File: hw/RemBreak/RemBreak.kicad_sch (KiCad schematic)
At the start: 4 parts, among them J1 Screw_Terminal_01x04, J2 Screw_Terminal_01x04

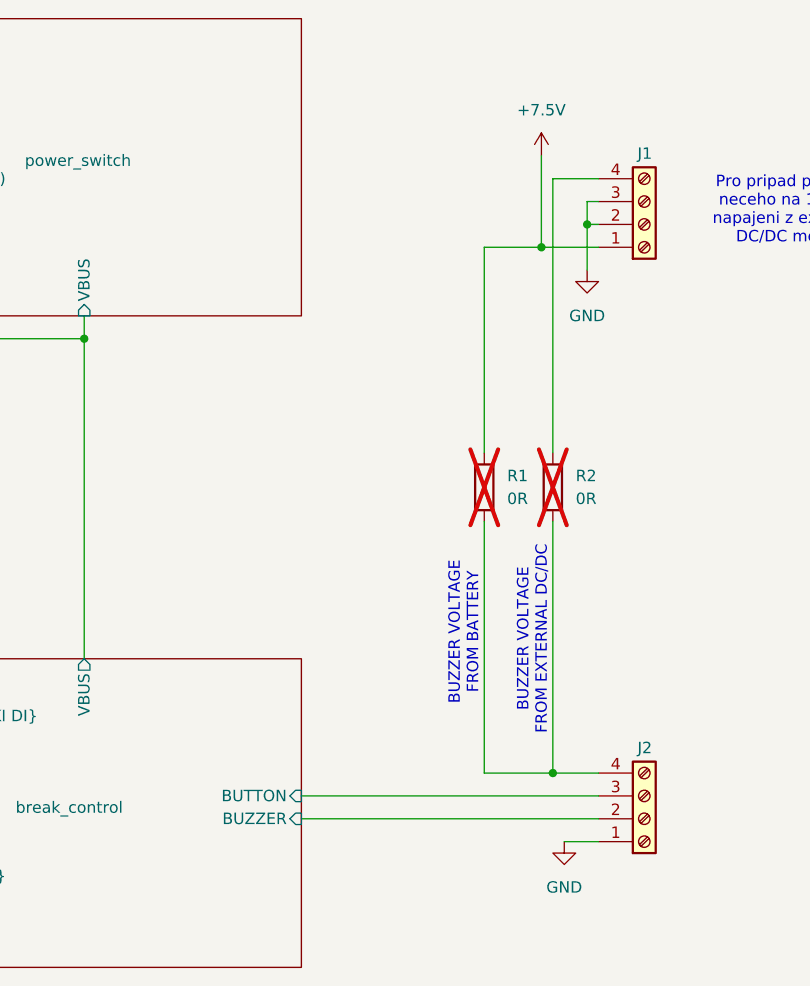
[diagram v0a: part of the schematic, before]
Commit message: partially reorganized components and routing
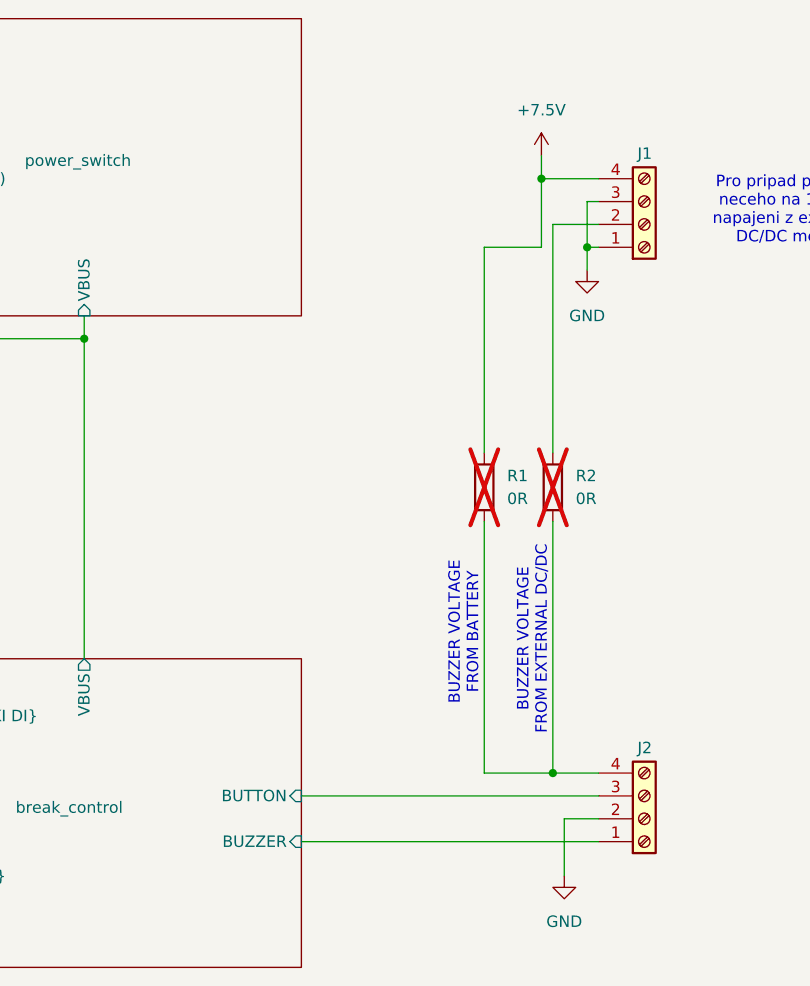
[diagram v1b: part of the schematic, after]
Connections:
- net +7.5V: now also J1.4 (Pin_4); no longer J1.1 (Pin_1)
- net GND: now also J1.1 (Pin_1), J2.2 (Pin_2); no longer J1.2 (Pin_2), J2.1 (Pin_1)
- net break_control/BUZZER: now also J2.1 (Pin_1); no longer J2.2 (Pin_2)
- net at R2.1: now also J1.2 (Pin_2); no longer J1.4 (Pin_4)
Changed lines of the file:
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@@
-	)
-	(junction
-		(at 234.95 68.58)
-		(diameter 0)
-		(color 0 0 0 0)
 	)
 	(junction
@@
 	)
 	(junction
-		(at 240.03 66.04)
+		(at 234.95 60.96)
 		(diameter 0)
 		(color 0 0 0 0)
@@
 	)
 	(junction
+		(at 240.03 68.58)
+		(diameter 0)
+		(color 0 0 0 0)
+	)
+	(junction
 		(at 236.22 127)
 		(diameter 0)
@@
 	(wire
 		(pts
+			(xy 208.28 134.62) (xy 241.3 134.62)
+		)
+		(stroke
+			(width 0)
+			(type default)
+		)
+	)
+	(wire
+		(pts
 			(xy 236.22 99.06) (xy 236.22 127)
 		)
@@
 	(wire
 		(pts
+			(xy 240.03 63.5) (xy 240.03 68.58)
+		)
+		(stroke
+			(width 0)
+			(type default)
+		)
+	)
+	(wire
+		(pts
 			(xy 82.55 129.54) (xy 161.29 129.54)
 		)
@@
 	(wire
 		(pts
-			(xy 234.95 68.58) (xy 241.3 68.58)
-		)
-		(stroke
-			(width 0)
-			(type default)
-		)
-	)
-	(wire
-		(pts
 			(xy 228.6 91.44) (xy 228.6 68.58)
 		)
@@
 	(wire
 		(pts
-			(xy 236.22 60.96) (xy 241.3 60.96)
-		)
-		(stroke
-			(width 0)
-			(type default)
-		)
-	)
-	(wire
-		(pts
-			(xy 240.03 66.04) (xy 240.03 63.5)
-		)
-		(stroke
-			(width 0)
-			(type default)
-		)
-	)
-	(wire
-		(pts
 			(xy 236.22 127) (xy 241.3 127)
 		)
@@
 	(wire
 		(pts
+			(xy 236.22 66.04) (xy 236.22 91.44)
+		)
+		(stroke
+			(width 0)
+			(type default)
+		)
+	)
+	(wire
+		(pts
+			(xy 240.03 68.58) (xy 241.3 68.58)
+		)
+		(stroke
+			(width 0)
+			(type default)
+		)
+	)
+	(wire
+		(pts
 			(xy 151.13 92.71) (xy 154.94 92.71)
 		)
@@
 	(wire
 		(pts
-			(xy 236.22 91.44) (xy 236.22 60.96)
+			(xy 234.95 60.96) (xy 241.3 60.96)
+		)
+		(stroke
+			(width 0)
+			(type default)
+		)
+	)
+	(wire
+		(pts
+			(xy 237.49 132.08) (xy 237.49 138.43)
 		)
 		(stroke
@@
 	(wire
 		(pts
+			(xy 234.95 60.96) (xy 234.95 68.58)
+		)
+		(stroke
+			(width 0)
+			(type default)
+		)
+	)
+	(wire
+		(pts
 			(xy 123.19 49.53) (xy 161.29 49.53)
 		)
@@
 	(wire
 		(pts
-			(xy 208.28 132.08) (xy 241.3 132.08)
-		)
-		(stroke
-			(width 0)
-			(type default)
-		)
-	)
-	(wire
-		(pts
-			(xy 234.95 58.42) (xy 234.95 68.58)
+			(xy 237.49 132.08) (xy 241.3 132.08)
+		)
+		(stroke
+			(width 0)
+			(type default)
+		)
+	)
+	(wire
+		(pts
+			(xy 234.95 58.42) (xy 234.95 60.96)
+		)
+		(stroke
+			(width 0)
+			(type default)
+		)
+	)
+	(wire
+		(pts
+			(xy 236.22 66.04) (xy 241.3 66.04)
 		)
 		(stroke
@@
 	(wire
 		(pts
-			(xy 237.49 134.62) (xy 241.3 134.62)
-		)
-		(stroke
-			(width 0)
-			(type default)
-		)
-	)
-	(wire
-		(pts
 			(xy 86.36 132.08) (xy 161.29 132.08)
 		)
@@
 	(wire
 		(pts
+			(xy 240.03 71.12) (xy 240.03 68.58)
+		)
+		(stroke
+			(width 0)
+			(type default)
+		)
+	)
+	(wire
+		(pts
 			(xy 86.36 92.71) (xy 86.36 132.08)
 		)
@@
 	(wire
 		(pts
-			(xy 240.03 71.12) (xy 240.03 66.04)
-		)
-		(stroke
-			(width 0)
-			(type default)
-		)
-	)
-	(wire
-		(pts
 			(xy 228.6 68.58) (xy 234.95 68.58)
 		)
@@
 		(pts
 			(xy 82.55 49.53) (xy 123.19 49.53)
-		)
-		(stroke
-			(width 0)
-			(type default)
-		)
-	)
-	(wire
-		(pts
-			(xy 240.03 66.04) (xy 241.3 66.04)
 		)
 		(stroke
@@
 	(symbol
 		(lib_id "power:GND")
-		(at 237.49 134.62 0)
+		(at 237.49 138.43 0)
 		(unit 1)
 		(exclude_from_sim no)
@@
 		(fields_autoplaced yes)
 		(property "Reference" "#PWR02"
-			(at 237.49 140.97 0)
+			(at 237.49 144.78 0)
 			(effects
 				(font
@@
 		)
 		(property "Value" "GND"
-			(at 237.49 139.7 0)
+			(at 237.49 143.51 0)
 			(effects
 				(font
@@
 		)
 		(property "Footprint" ""
-			(at 237.49 134.62 0)
+			(at 237.49 138.43 0)
 			(effects
 				(font
@@
 		)
 		(property "Datasheet" ""
-			(at 237.49 134.62 0)
+			(at 237.49 138.43 0)
 			(effects
 				(font
@@
 		)
 		(property "Description" "Power symbol creates a global label with name \"GND\" , ground"
-			(at 237.49 134.62 0)
+			(at 237.49 138.43 0)
 			(effects
 				(font
@@
 		)
 		(pin "BUZZER" input
-			(at 208.28 132.08 0)
-			(effects
-				(font
+			(at 208.28 134.62 0)
+			(effects
+				(font

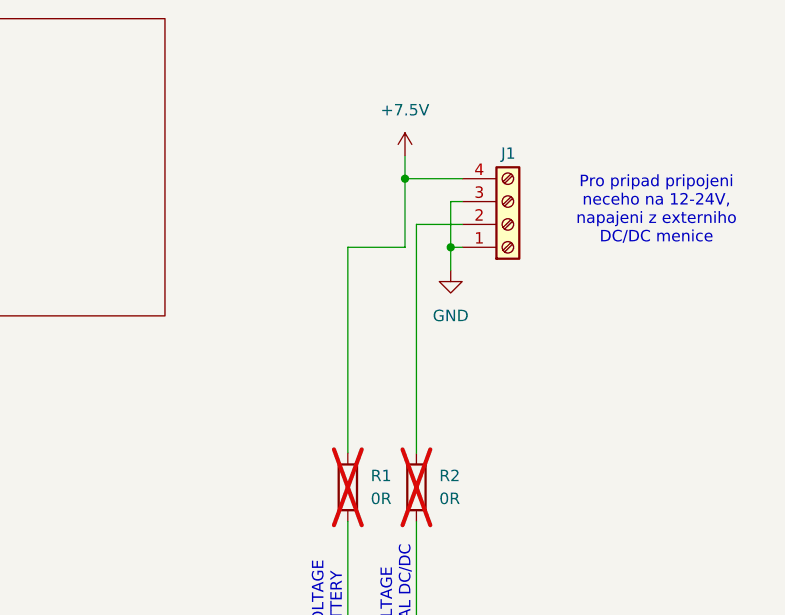
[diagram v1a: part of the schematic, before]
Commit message: middle part rerouted to fix the gnd connection
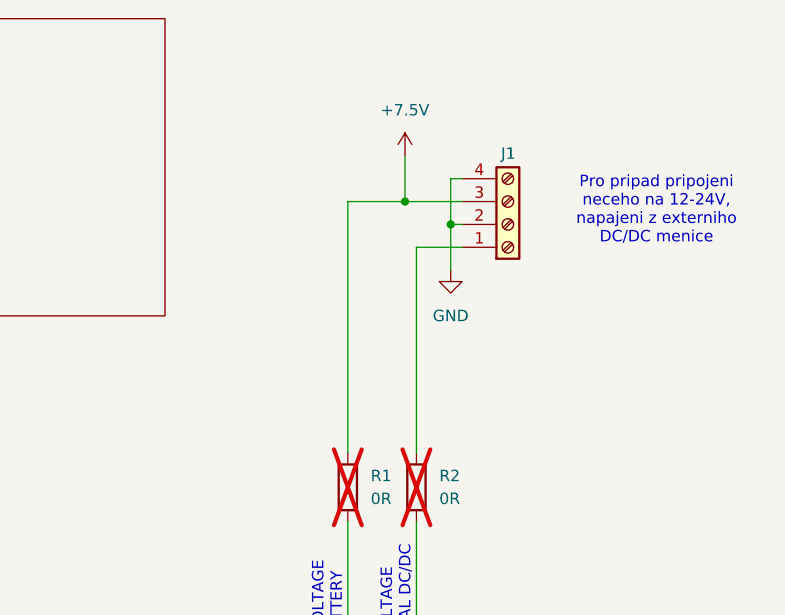
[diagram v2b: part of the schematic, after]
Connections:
- net +7.5V: now also J1.3 (Pin_3); no longer J1.4 (Pin_4)
- net GND: now also J1.2 (Pin_2), J1.4 (Pin_4); no longer J1.1 (Pin_1), J1.3 (Pin_3)
- net at R2.1: now also J1.1 (Pin_1); no longer J1.2 (Pin_2)
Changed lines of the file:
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@@
+	)
+	(junction
+		(at 234.95 63.5)
+		(diameter 0)
+		(color 0 0 0 0)
 	)
 	(junction
@@
 	)
 	(junction
-		(at 234.95 60.96)
-		(diameter 0)
-		(color 0 0 0 0)
-	)
-	(junction
 		(at 184.15 78.74)
 		(diameter 0)
@@
 	)
 	(junction
-		(at 240.03 68.58)
-		(diameter 0)
-		(color 0 0 0 0)
-	)
-	(junction
 		(at 236.22 127)
 		(diameter 0)
 		(color 0 0 0 0)
 	)
+	(junction
+		(at 240.03 66.04)
+		(diameter 0)
+		(color 0 0 0 0)
+	)
 	(wire
 		(pts
@@
 	(wire
 		(pts
-			(xy 240.03 63.5) (xy 240.03 68.58)
+			(xy 240.03 60.96) (xy 241.3 60.96)
 		)
 		(stroke
@@
 	(wire
 		(pts
-			(xy 228.6 91.44) (xy 228.6 68.58)
-		)
-		(stroke
-			(width 0)
-			(type default)
-		)
-	)
-	(wire
-		(pts
 			(xy 228.6 127) (xy 236.22 127)
 		)
@@
 	(wire
 		(pts
-			(xy 236.22 66.04) (xy 236.22 91.44)
-		)
-		(stroke
-			(width 0)
-			(type default)
-		)
-	)
-	(wire
-		(pts
-			(xy 240.03 68.58) (xy 241.3 68.58)
-		)
-		(stroke
-			(width 0)
-			(type default)
-		)
-	)
-	(wire
-		(pts
 			(xy 151.13 92.71) (xy 154.94 92.71)
 		)
@@
 		)
 	)
+	(wire
+		(pts
+			(xy 240.03 66.04) (xy 241.3 66.04)
+		)
+		(stroke
+			(width 0)
+			(type default)
+		)
+	)
+	(wire
+		(pts
+			(xy 240.03 66.04) (xy 240.03 60.96)
+		)
+		(stroke
+			(width 0)
+			(type default)
+		)
+	)
+	(wire
+		(pts
+			(xy 236.22 68.58) (xy 241.3 68.58)
+		)
+		(stroke
+			(width 0)
+			(type default)
+		)
+	)
 	(bus
 		(pts
@@
 	(wire
 		(pts
-			(xy 234.95 60.96) (xy 241.3 60.96)
+			(xy 240.03 71.12) (xy 240.03 66.04)
 		)
 		(stroke
@@
 		)
 	)
+	(wire
+		(pts
+			(xy 228.6 63.5) (xy 228.6 91.44)
+		)
+		(stroke
+			(width 0)
+			(type default)
+		)
+	)
 	(bus
 		(pts
@@
 	(wire
 		(pts
-			(xy 234.95 60.96) (xy 234.95 68.58)
-		)
-		(stroke
-			(width 0)
-			(type default)
-		)
-	)
-	(wire
-		(pts
 			(xy 123.19 49.53) (xy 161.29 49.53)
 		)
@@
 	(wire
 		(pts
-			(xy 234.95 58.42) (xy 234.95 60.96)
-		)
-		(stroke
-			(width 0)
-			(type default)
-		)
-	)
-	(wire
-		(pts
-			(xy 236.22 66.04) (xy 241.3 66.04)
+			(xy 234.95 58.42) (xy 234.95 63.5)
 		)
 		(stroke
@@
 	(wire
 		(pts
+			(xy 228.6 63.5) (xy 234.95 63.5)
+		)
+		(stroke
+			(width 0)
+			(type default)
+		)
+	)
+	(wire
+		(pts
 			(xy 86.36 132.08) (xy 161.29 132.08)
 		)
@@
 	(wire
 		(pts
-			(xy 240.03 71.12) (xy 240.03 68.58)
-		)
-		(stroke
-			(width 0)
-			(type default)
-		)
-	)
-	(wire
-		(pts
 			(xy 86.36 92.71) (xy 86.36 132.08)
 		)
@@
 	(wire
 		(pts
-			(xy 228.6 68.58) (xy 234.95 68.58)
-		)
-		(stroke
-			(width 0)
-			(type default)
-		)
-	)
-	(wire
-		(pts
 			(xy 123.19 49.53) (xy 123.19 82.55)
 		)
@@
 	(wire
 		(pts
+			(xy 236.22 68.58) (xy 236.22 91.44)
+		)
+		(stroke
+			(width 0)
+			(type default)
+		)
+	)
+	(wire
+		(pts
 			(xy 82.55 78.74) (xy 184.15 78.74)
 		)
@@
 	(wire
 		(pts
-			(xy 240.03 63.5) (xy 241.3 63.5)
-		)
-		(stroke
-			(width 0)
-			(type default)
-		)
-	)
-	(wire
-		(pts
 			(xy 228.6 127) (xy 228.6 99.06)
 		)
@@
 		)
 		(stroke
+			(width 0)
+			(type default)
+		)
+	)
+	(wire
+		(pts
+			(xy 234.95 63.5) (xy 241.3 63.5)
+		)
+		(stroke

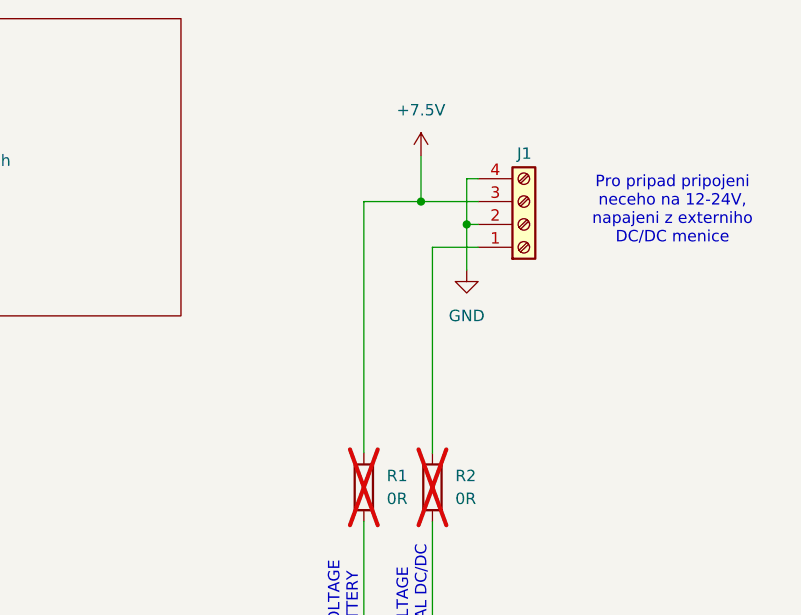
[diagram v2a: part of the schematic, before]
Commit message: finished routing - drc did not pass
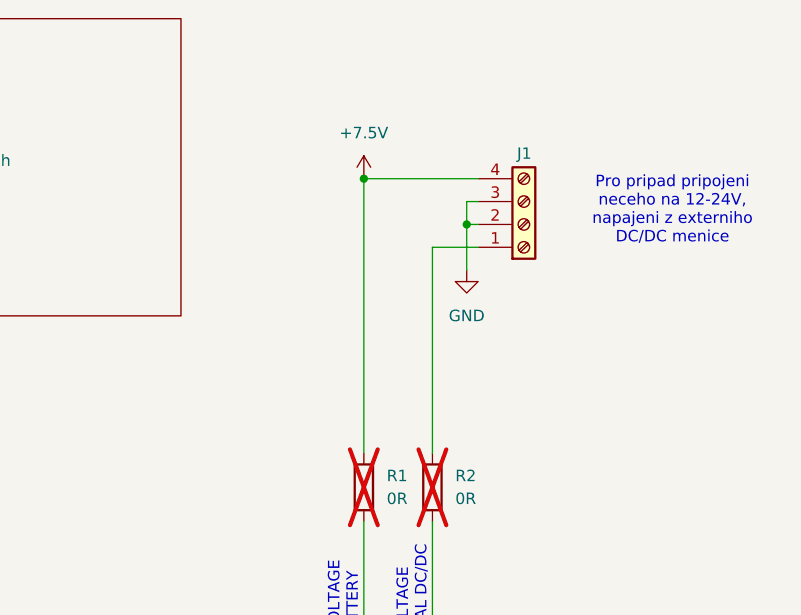
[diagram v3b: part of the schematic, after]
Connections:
- net +7.5V: now also J1.4 (Pin_4); no longer J1.3 (Pin_3)
- net GND: now also J1.3 (Pin_3); no longer J1.4 (Pin_4)
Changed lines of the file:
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@@
 	)
 	(junction
-		(at 234.95 63.5)
+		(at 240.03 66.04)
 		(diameter 0)
 		(color 0 0 0 0)
@@
 	)
 	(junction
+		(at 228.6 60.96)
+		(diameter 0)
+		(color 0 0 0 0)
+	)
+	(junction
 		(at 184.15 78.74)
 		(diameter 0)
@@
 		(color 0 0 0 0)
 	)
-	(junction
-		(at 240.03 66.04)
-		(diameter 0)
-		(color 0 0 0 0)
-	)
 	(wire
 		(pts
@@
 	(wire
 		(pts
-			(xy 240.03 60.96) (xy 241.3 60.96)
+			(xy 241.3 63.5) (xy 240.03 63.5)
 		)
 		(stroke
@@
 	(wire
 		(pts
+			(xy 240.03 63.5) (xy 240.03 66.04)
+		)
+		(stroke
+			(width 0)
+			(type default)
+		)
+	)
+	(wire
+		(pts
 			(xy 228.6 127) (xy 236.22 127)
 		)
@@
 	(wire
 		(pts
-			(xy 240.03 66.04) (xy 240.03 60.96)
-		)
-		(stroke
-			(width 0)
-			(type default)
-		)
-	)
-	(wire
-		(pts
 			(xy 236.22 68.58) (xy 241.3 68.58)
 		)
@@
 	(wire
 		(pts
-			(xy 228.6 63.5) (xy 228.6 91.44)
+			(xy 228.6 60.96) (xy 228.6 91.44)
 		)
 		(stroke
@@
 		)
 	)
-	(wire
-		(pts
-			(xy 234.95 58.42) (xy 234.95 63.5)
-		)
-		(stroke
-			(width 0)
-			(type default)
-		)
-	)
 	(bus
 		(pts
@@
 	(wire
 		(pts
-			(xy 228.6 63.5) (xy 234.95 63.5)
-		)
-		(stroke
-			(width 0)
-			(type default)
-		)
-	)
-	(wire
-		(pts
 			(xy 86.36 132.08) (xy 161.29 132.08)
 		)
@@
 	(wire
 		(pts
+			(xy 241.3 60.96) (xy 228.6 60.96)
+		)
+		(stroke
+			(width 0)
+			(type default)
+		)
+	)
+	(wire
+		(pts
 			(xy 82.55 88.9) (xy 93.98 88.9)
 		)
@@
 		(pts
 			(xy 184.15 78.74) (xy 184.15 114.3)
-		)
-		(stroke
-			(width 0)
-			(type default)
-		)
-	)
-	(wire
-		(pts
-			(xy 234.95 63.5) (xy 241.3 63.5)
 		)
 		(stroke
@@
 	(symbol
 		(lib_id "power:+7.5V")
-		(at 234.95 58.42 0)
+		(at 228.6 60.96 0)
 		(unit 1)
 		(exclude_from_sim no)
@@
 		(fields_autoplaced yes)
 		(property "Reference" "#PWR01"
-			(at 234.95 62.23 0)
+			(at 228.6 64.77 0)
 			(effects
 				(font
@@
 		)
 		(property "Value" "+7.5V"
-			(at 234.95 53.34 0)
+			(at 228.6 55.88 0)
 			(effects
 				(font
@@
 		)
 		(property "Footprint" ""
-			(at 234.95 58.42 0)
+			(at 228.6 60.96 0)
 			(effects
 				(font
@@
 		)
 		(property "Datasheet" ""
-			(at 234.95 58.42 0)
+			(at 228.6 60.96 0)
 			(effects
 				(font
@@
 		)
 		(property "Description" "Power symbol creates a global label with name \"+7.5V\""
-			(at 234.95 58.42 0)
-			(effects
-				(font
+			(at 228.6 60.96 0)
+			(effects
+				(font
